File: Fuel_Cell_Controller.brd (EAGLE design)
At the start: 203.2 x 163.8 mm, 83 parts, among them J1 BLUETOOTH, U1 MAX232PTH

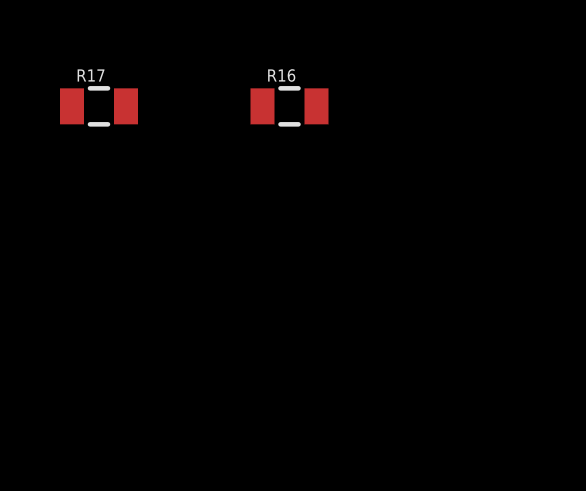
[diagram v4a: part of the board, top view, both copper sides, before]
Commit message: Added a couple indicator LED's and speced out parts on digikey. Added connections to NUCLEO. Will create a part for the RGB LED next and implement it
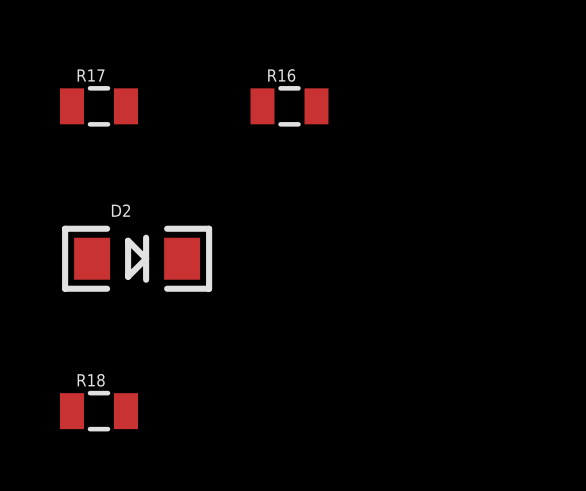
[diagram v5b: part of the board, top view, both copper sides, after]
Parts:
- added D2: YELLOW, SparkFun-LED:LED-1206
- added R18: 324Ω, SparkFun-Passives:0805
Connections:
- net DEBUG_MODE renamed START_LED
- net N$20 renamed SHUT_LED
- removed net N$19: U$1.PG_1
- removed net RUN_MODE: U$1.PG_0
- new net ALARM_LED: R13.1, U$1.PG_0
- new net DEBUG_LED: R18.1, U$1.PG_1
- new net N$17: D2.A, R18.2
- new net RUN_LED: U$1.PG_9
- net 3V3: no longer R13.1
- net GND: now also D2.C
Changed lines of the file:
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@@
 <element name="R16" library="SparkFun-Passives" package="0805" value="10kΩ" x="-26.67" y="-138.43"/>
 <element name="R17" library="SparkFun-Passives" package="0805" value="10kΩ" x="-33.02" y="-138.43"/>
+<element name="D2" library="SparkFun-LED" package="LED-1206" value="YELLOW" x="-31.75" y="-143.51"/>
+<element name="R18" library="SparkFun-Passives" package="0805" value="324Ω" x="-33.02" y="-148.59"/>
 </elements>
 <signals>
@@
 <contactref element="U$3" pad="11"/>
 <contactref element="R17" pad="1"/>
+<contactref element="D2" pad="C"/>
 <wire x1="107.0864" y1="147.32" x2="113.03" y2="139.7" width="0" layer="19" extent="1-1"/>
 <wire x1="107.95" y1="129.17" x2="113.03" y2="139.7" width="0" layer="19" extent="1-1"/>
@@
 <wire x1="-25.77" y1="-99.06" x2="-25.77" y2="-95.25" width="0" layer="19" extent="1-1"/>
 <wire x1="-33.92" y1="-138.43" x2="-25.77" y2="-99.06" width="0" layer="19" extent="1-1"/>
+<wire x1="-30.25" y1="-143.51" x2="-33.92" y2="-138.43" width="0" layer="19" extent="1-1"/>
 </signal>
 <signal name="+5V">
@@
 <contactref element="U$20" pad="VDD"/>
 <contactref element="C6" pad="1"/>
-<contactref element="R13" pad="1"/>
 <contactref element="U$24" pad="D"/>
 <contactref element="R16" pad="1"/>
@@
 <wire x1="82.55" y1="116.84" x2="95.25" y2="111.76" width="0" layer="19" extent="1-1"/>
 <wire x1="16.51" y1="85.730715625" x2="82.55" y2="116.84" width="0" layer="19" extent="1-1"/>
-<wire x1="-18.68" y1="-27.94" x2="16.51" y2="85.730715625" width="0" layer="19" extent="1-1"/>
-<wire x1="-18.1" y1="-44.72" x2="-18.68" y2="-27.94" width="0" layer="19" extent="1-1"/>
+<wire x1="-18.1" y1="-44.72" x2="16.51" y2="85.730715625" width="0" layer="19" extent="1-1"/>
 <wire x1="-27.52" y1="-66.04" x2="-18.1" y2="-44.72" width="0" layer="19" extent="1-1"/>
 <wire x1="-26.67" y1="-126" x2="-27.52" y2="-66.04" width="0" layer="19" extent="1-1"/>
@@
 <wire x1="-20.55" y1="-24.13" x2="-16.88" y2="-27.94" width="0" layer="19" extent="1-1"/>
 </signal>
-<signal name="RUN_MODE">
+<signal name="ALARM_LED">
 <contactref element="U$1" pad="PG_0"/>
-</signal>
-<signal name="N$19">
+<contactref element="R13" pad="1"/>
+<wire x1="-18.68" y1="-27.94" x2="16.51" y2="34.930715625" width="0" layer="19" extent="1-1"/>
+</signal>
+<signal name="DEBUG_LED">
 <contactref element="U$1" pad="PG_1"/>
-</signal>
-<signal name="N$20">
+<contactref element="R18" pad="1"/>
+<wire x1="19.05" y1="34.930715625" x2="-33.92" y2="-148.59" width="0" layer="19" extent="1-1"/>
+</signal>
+<signal name="SHUT_LED">
 <contactref element="U$1" pad="PG_2"/>
 </signal>
@@
 <wire x1="-32.12" y1="-138.43" x2="-25.72" y2="-128" width="0" layer="19" extent="1-1"/>
 </signal>
-<signal name="DEBUG_MODE">
+<signal name="START_LED">
 <contactref element="U$1" pad="PG_3"/>
 </signal>
@@
 <wire x1="16.51" y1="45.090715625" x2="16.51" y2="47.630715625" width="0" layer="19" extent="1-1"/>
 </signal>
+<signal name="RUN_LED">
+<contactref element="U$1" pad="PG_9"/>
+</signal>
+<signal name="N$17">
+<contactref element="R18" pad="2"/>
+<contactref element="D2" pad="A"/>
+<wire x1="-33.25" y1="-143.51" x2="-32.12" y2="-148.59" width="0" layer="19" extent="1-1"/>
+</signal>
 </signals>

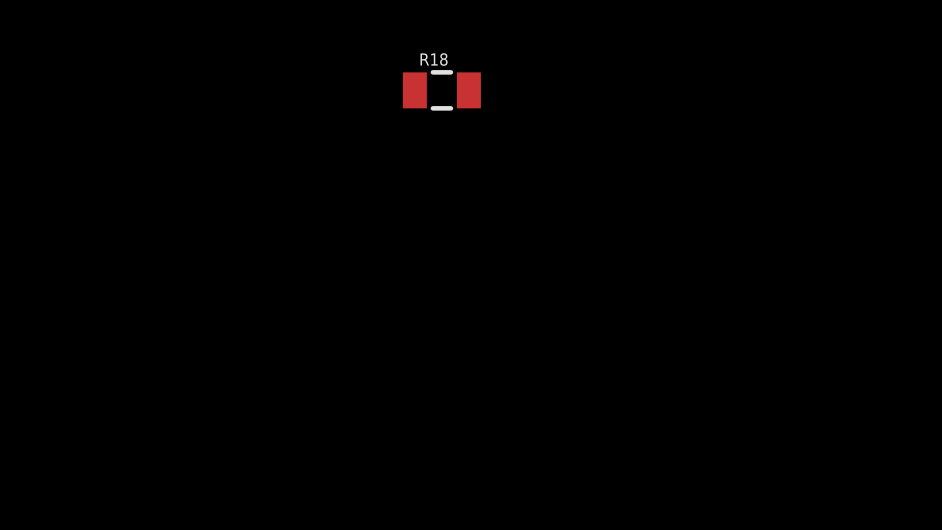
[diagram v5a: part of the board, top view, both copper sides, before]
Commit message: Implemented all indicator LED's, including the RGB one
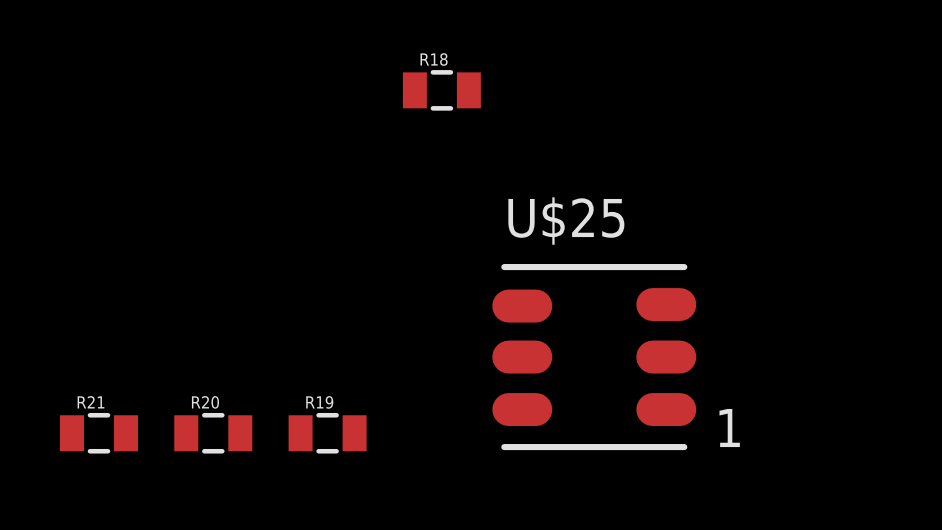
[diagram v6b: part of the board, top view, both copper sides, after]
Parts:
- added R19, R20, R21: 324Ω, SparkFun-Passives:0805
- added U$25: 5060BRG45060BRG4, FCC_parts:5060BRG4
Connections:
- new net N$18: R19.2, U$25.1
- new net N$19: R20.2, U$25.2
- new net N$20: R21.2, U$25.3
- net GND: now also U$25.4, U$25.5, U$25.6
- net RUN_LED: now also R19.1
- net SHUT_LED: now also R20.1
- net START_LED: now also R21.1
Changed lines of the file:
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@@
 <element name="D2" library="SparkFun-LED" package="LED-1206" value="YELLOW" x="-31.75" y="-143.51"/>
 <element name="R18" library="SparkFun-Passives" package="0805" value="324Ω" x="-33.02" y="-148.59"/>
+<element name="U$25" library="FCC_parts" package="5060BRG4" value="5060BRG45060BRG4" x="-27.94" y="-157.48"/>
+<element name="R19" library="SparkFun-Passives" package="0805" value="324Ω" x="-36.83" y="-160.02"/>
+<element name="R20" library="SparkFun-Passives" package="0805" value="324Ω" x="-40.64" y="-160.02"/>
+<element name="R21" library="SparkFun-Passives" package="0805" value="324Ω" x="-44.45" y="-160.02"/>
 </elements>
 <signals>
@@
 <contactref element="ETH1" pad="P$7"/>
 <contactref element="ETH4" pad="P$8"/>
-<contactref element="D1" pad="C"/>
 <contactref element="U$20" pad="GND"/>
 <contactref element="U$21" pad="A1"/>
@@
 <contactref element="U$3" pad="11"/>
 <contactref element="R17" pad="1"/>
+<contactref element="D1" pad="C"/>
 <contactref element="D2" pad="C"/>
+<contactref element="U$25" pad="6"/>
+<contactref element="U$25" pad="5"/>
+<contactref element="U$25" pad="4"/>
 <wire x1="107.0864" y1="147.32" x2="113.03" y2="139.7" width="0" layer="19" extent="1-1"/>
 <wire x1="107.95" y1="129.17" x2="113.03" y2="139.7" width="0" layer="19" extent="1-1"/>
@@
 <wire x1="-33.92" y1="-138.43" x2="-25.77" y2="-99.06" width="0" layer="19" extent="1-1"/>
 <wire x1="-30.25" y1="-143.51" x2="-33.92" y2="-138.43" width="0" layer="19" extent="1-1"/>
+<wire x1="-30.34" y1="-155.78" x2="-30.25" y2="-143.51" width="0" layer="19" extent="1-1"/>
+<wire x1="-30.34" y1="-157.48" x2="-30.34" y2="-155.78" width="0" layer="19" extent="1-1"/>
+<wire x1="-30.34" y1="-159.23" x2="-30.34" y2="-157.48" width="0" layer="19" extent="1-1"/>
 </signal>
 <signal name="+5V">
@@
 <signal name="SHUT_LED">
 <contactref element="U$1" pad="PG_2"/>
+<contactref element="R20" pad="1"/>
+<wire x1="19.05" y1="78.110715625" x2="-41.54" y2="-160.02" width="0" layer="19" extent="1-1"/>
 </signal>
 <signal name="OE*">
@@
 <signal name="START_LED">
 <contactref element="U$1" pad="PG_3"/>
+<contactref element="R21" pad="1"/>
+<wire x1="19.05" y1="75.570715625" x2="-45.35" y2="-160.02" width="0" layer="19" extent="1-1"/>
 </signal>
 <signal name="INTERRUPT">
@@
 <signal name="RUN_LED">
 <contactref element="U$1" pad="PG_9"/>
+<contactref element="R19" pad="1"/>
+<wire x1="64.77" y1="57.790715625" x2="-37.73" y2="-160.02" width="0" layer="19" extent="1-1"/>
 </signal>
 <signal name="N$17">
@@
 <wire x1="-33.25" y1="-143.51" x2="-32.12" y2="-148.59" width="0" layer="19" extent="1-1"/>
 </signal>
+<signal name="N$18">
+<contactref element="U$25" pad="1"/>
+<contactref element="R19" pad="2"/>
+<wire x1="-25.54" y1="-159.23" x2="-35.93" y2="-160.02" width="0" layer="19" extent="1-1"/>
+</signal>
+<signal name="N$19">
+<contactref element="U$25" pad="2"/>
+<contactref element="R20" pad="2"/>
+<wire x1="-25.54" y1="-157.48" x2="-39.74" y2="-160.02" width="0" layer="19" extent="1-1"/>
+</signal>
+<signal name="N$20">
+<contactref element="U$25" pad="3"/>
+<contactref element="R21" pad="2"/>
+<wire x1="-25.54" y1="-155.73" x2="-43.55" y2="-160.02" width="0" layer="19" extent="1-1"/>
+</signal>
 </signals>

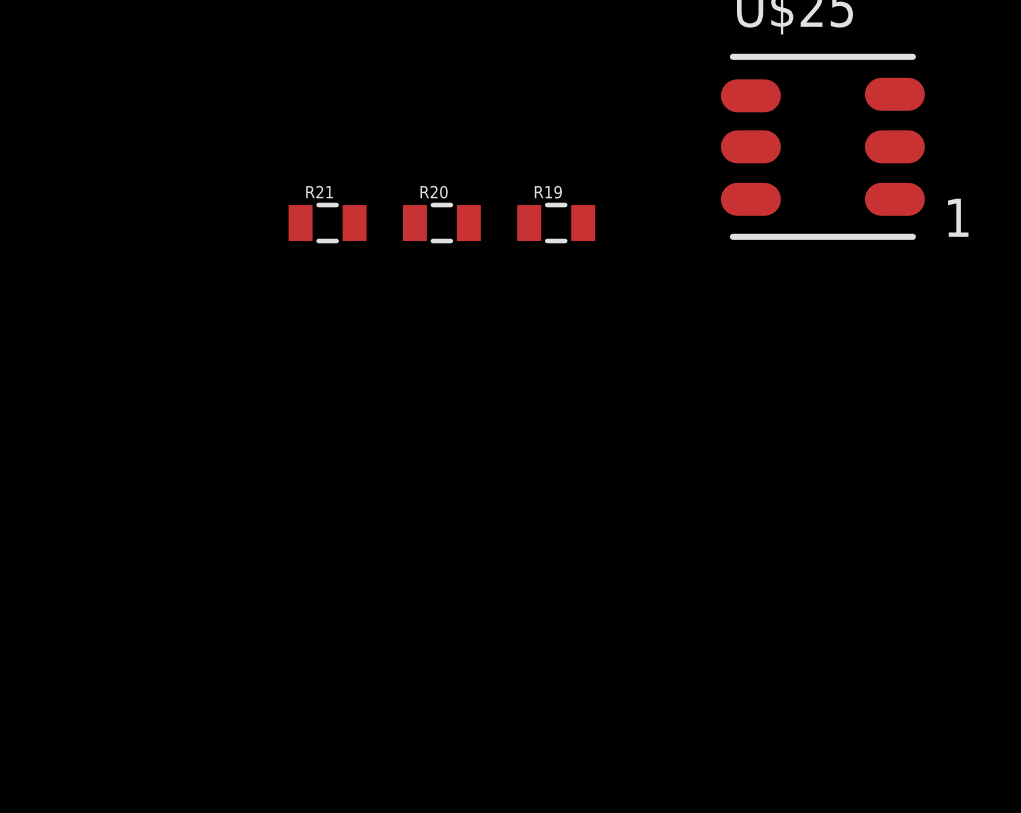
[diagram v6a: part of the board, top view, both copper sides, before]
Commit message: Added another screw terminal and voltage division for mass flow meter and connected it to the external ADC
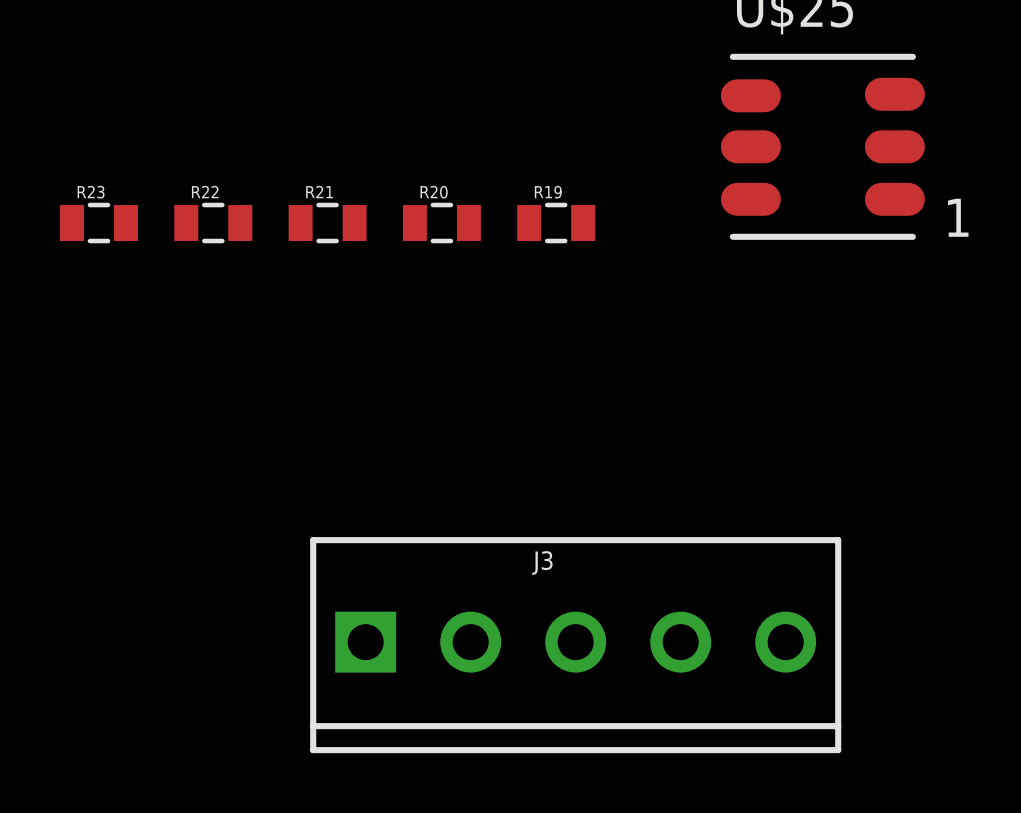
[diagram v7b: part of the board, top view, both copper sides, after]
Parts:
- added J3: (no value), SparkFun-Connectors:SCREWTERMINAL-3.5MM-5
- added R22, R23: 1kΩ, SparkFun-Passives:0805
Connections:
- removed net ADC_A0: J2.2, U$19.P$7
- new net N$22: R22.2, X1.3
- net GND: now also J3.1, R23.1
- net MASS_FLOW: now also R22.1, R23.2, U$19.P$7; no longer X1.3
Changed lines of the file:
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@@
 <element name="R20" library="SparkFun-Passives" package="0805" value="324Ω" x="-40.64" y="-160.02"/>
 <element name="R21" library="SparkFun-Passives" package="0805" value="324Ω" x="-44.45" y="-160.02"/>
+<element name="R22" library="SparkFun-Passives" package="0805" value="1kΩ" x="-48.26" y="-160.02"/>
+<element name="R23" library="SparkFun-Passives" package="0805" value="1kΩ" x="-52.07" y="-160.02"/>
+<element name="J3" library="SparkFun-Connectors" library_urn="urn:adsk.eagle:library:513" package="SCREWTERMINAL-3.5MM-5" package3d_urn="urn:adsk.eagle:package:38112/1" value="" x="-43.18" y="-173.99">
+<attribute name="PROD_ID" value="Combine 8288+8399" x="-43.18" y="-173.99" size="1.778" layer="27" display="off"/>
+</element>
 </elements>
 <signals>
@@
 <contactref element="U$25" pad="5"/>
 <contactref element="U$25" pad="4"/>
+<contactref element="R23" pad="1"/>
+<contactref element="J3" pad="1"/>
 <wire x1="107.0864" y1="147.32" x2="113.03" y2="139.7" width="0" layer="19" extent="1-1"/>
 <wire x1="107.95" y1="129.17" x2="113.03" y2="139.7" width="0" layer="19" extent="1-1"/>
@@
 <wire x1="-30.34" y1="-157.48" x2="-30.34" y2="-155.78" width="0" layer="19" extent="1-1"/>
 <wire x1="-30.34" y1="-159.23" x2="-30.34" y2="-157.48" width="0" layer="19" extent="1-1"/>
+<wire x1="-43.18" y1="-173.99" x2="-30.34" y2="-159.23" width="0" layer="19" extent="1-1"/>
+<wire x1="-52.97" y1="-160.02" x2="-43.18" y2="-173.99" width="0" layer="19" extent="1-1"/>
 </signal>
 <signal name="+5V">
@@
 <wire x1="154.57" y1="110.49" x2="130.81" y2="72.39" width="0" layer="19" extent="1-1"/>
 </signal>
-<signal name="MASS_FLOW">
-<contactref element="X1" pad="3"/>
-</signal>
 <signal name="I2C1_SDA">
 <contactref element="U$18" pad="P$4"/>
@@
 <wire x1="82.55" y1="109.22" x2="146.05" y2="91.44" width="0" layer="19" extent="1-1"/>
 <wire x1="64.77" y1="100.970715625" x2="82.55" y2="109.22" width="0" layer="19" extent="1-1"/>
-</signal>
-<signal name="ADC_A0">
-<contactref element="U$19" pad="P$7"/>
-<contactref element="J2" pad="2"/>
-<wire x1="120.65" y1="96.52" x2="117.8" y2="116.84" width="0" layer="19" extent="1-1"/>
 </signal>
 <signal name="ADC_A1">
@@
 <wire x1="-25.54" y1="-155.73" x2="-43.55" y2="-160.02" width="0" layer="19" extent="1-1"/>
 </signal>
+<signal name="MASS_FLOW">
+<contactref element="R22" pad="1"/>
+<contactref element="R23" pad="2"/>
+<contactref element="U$19" pad="P$7"/>
+<wire x1="-49.16" y1="-160.02" x2="120.65" y2="96.52" width="0" layer="19" extent="1-1"/>
+<wire x1="-51.17" y1="-160.02" x2="-49.16" y2="-160.02" width="0" layer="19" extent="1-1"/>
+</signal>
+<signal name="N$22">
+<contactref element="X1" pad="3"/>
+<contactref element="R22" pad="2"/>
+<wire x1="135.89" y1="147.32" x2="-47.36" y2="-160.02" width="0" layer="19" extent="1-1"/>
+</signal>
 </signals>

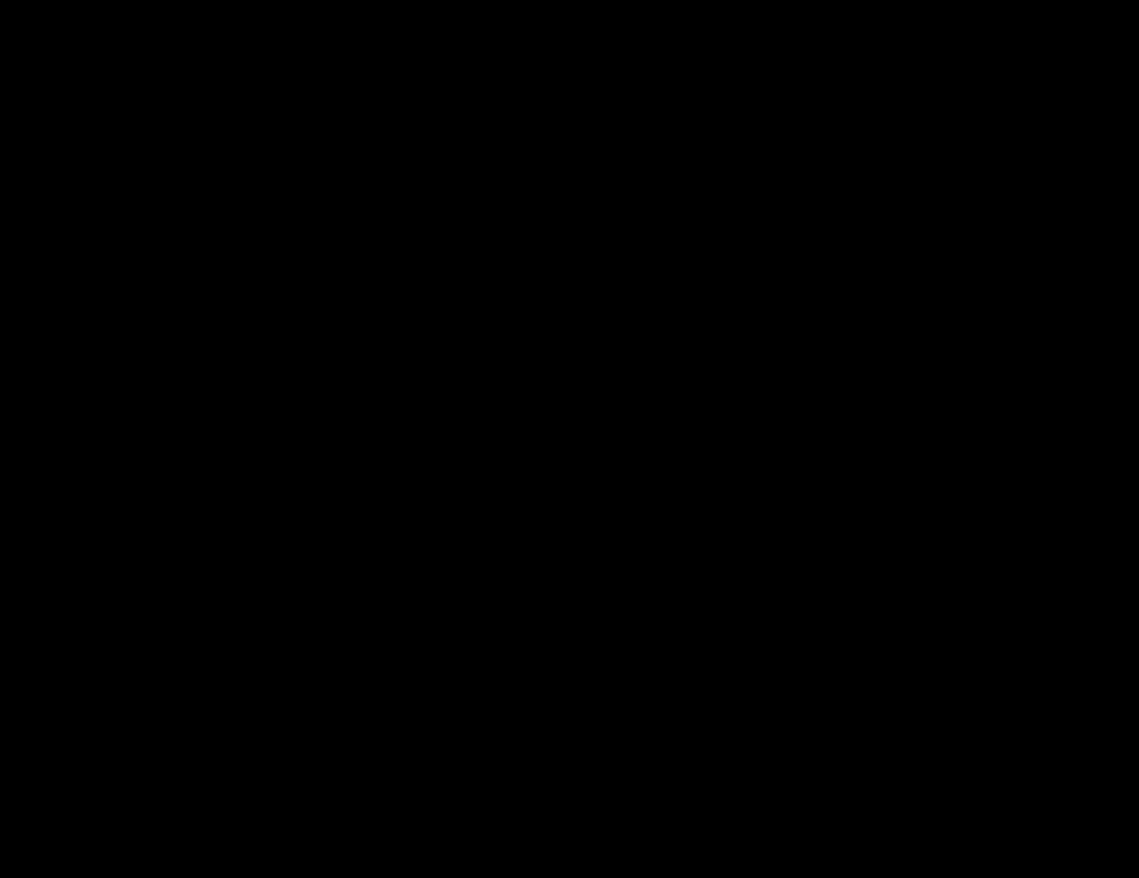
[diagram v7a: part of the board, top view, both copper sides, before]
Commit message: Added extra backup rs232 port
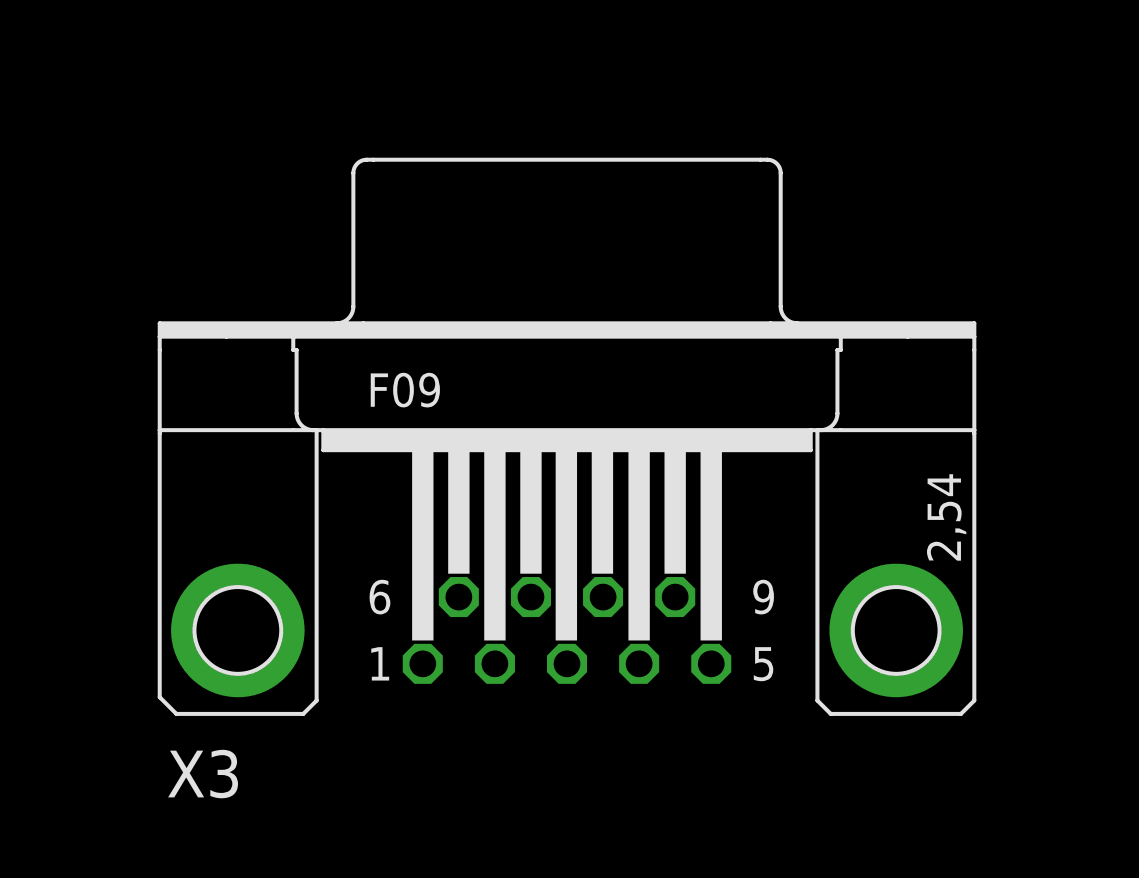
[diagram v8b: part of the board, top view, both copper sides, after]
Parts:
- added X3: (no value), con-subd:F09HP
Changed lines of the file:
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@@
 <attribute name="PROD_ID" value="Combine 8288+8399" x="-43.18" y="-173.99" size="1.778" layer="27" display="off"/>
+</element>
+<element name="X3" library="con-subd" library_urn="urn:adsk.eagle:library:189" package="F09HP" package3d_urn="urn:adsk.eagle:package:10232/1" value="" x="-15.24" y="-209.55">
+<attribute name="MF" value="" x="-15.24" y="-209.55" size="1.778" layer="27" display="off"/>
+<attribute name="MPN" value="" x="-15.24" y="-209.55" size="1.778" layer="27" display="off"/>
+<attribute name="OC_FARNELL" value="unknown" x="-15.24" y="-209.55" size="1.778" layer="27" display="off"/>
+<attribute name="OC_NEWARK" value="unknown" x="-15.24" y="-209.55" size="1.778" layer="27" display="off"/>
 </element>
 </elements>
